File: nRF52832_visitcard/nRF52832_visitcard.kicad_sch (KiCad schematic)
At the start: 65 parts, among them J1 Programming, J2 UART, SW1 SW_Push, Y1 32 MHz

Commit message: Added LCSC to all the components
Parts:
- BT1: LCSC (none) -> C70373
- C1, C4, C8: LCSC (none) -> C1525
- C10: LCSC (none) -> C1705
- C11: footprint Capacitor_SMD:C_0402_1005Metric_Pad0.74x0.62mm_HandSolder -> Capacitor_SMD:C_0805_2012Metric_Pad1.18x1.45mm_HandSolder; LCSC (none) -> C1711
- C12: LCSC (none) -> C1691
- C13, C14: LCSC (none) -> C1546
- C2: LCSC (none) -> C23687
- C3: LCSC (none) -> C15684
- C5, C6: LCSC (none) -> C26406
- C7: LCSC (none) -> C126516
- C9: LCSC (none) -> C1606
- D1, D10, D11, D12, D13, D14, D15, D16, D17, D18, D2, D3, D4, D5, D6, D7, D8, D9: LCSC (none) -> C5197644
- L1: LCSC (none) -> C51942
- L2: LCSC (none) -> C23651
- L3: LCSC (none) -> C90202
- R1, R2: LCSC (none) -> C25992
- R10, R11, R12, R13, R14, R15, R16, R17, R18, R19, R20, R3, R4, R5, R6, R7, R8, R9: LCSC (none) -> C14676
- R21: LCSC (none) -> C15401
- U1: LCSC (none) -> C77540
- U2: LCSC (none) -> C976032
- Y1: LCSC (none) -> C5830663

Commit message: LCSC added to another component
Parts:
- SW1: LCSC (none) -> C499301
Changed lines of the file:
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@@
+      (effects (font (size 1.27 1.27)) hide)
+    )
+    (property "LCSC" "C499301" (at 201.93 138.43 90)
       (effects (font (size 1.27 1.27)) hide)
     )

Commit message: Board layout fix
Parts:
- C15: now not fitted
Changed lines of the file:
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@@
   )
   (symbol (lib_id "Device:C") (at 143.51 139.7 0) (unit 1)
-    (in_bom yes) (on_board yes) (dnp no)
+    (in_bom yes) (on_board yes) (dnp yes)
     (property "Reference" "C15" (at 139.7 139.7 90)
       (effects (font (size 1.27 1.27)))

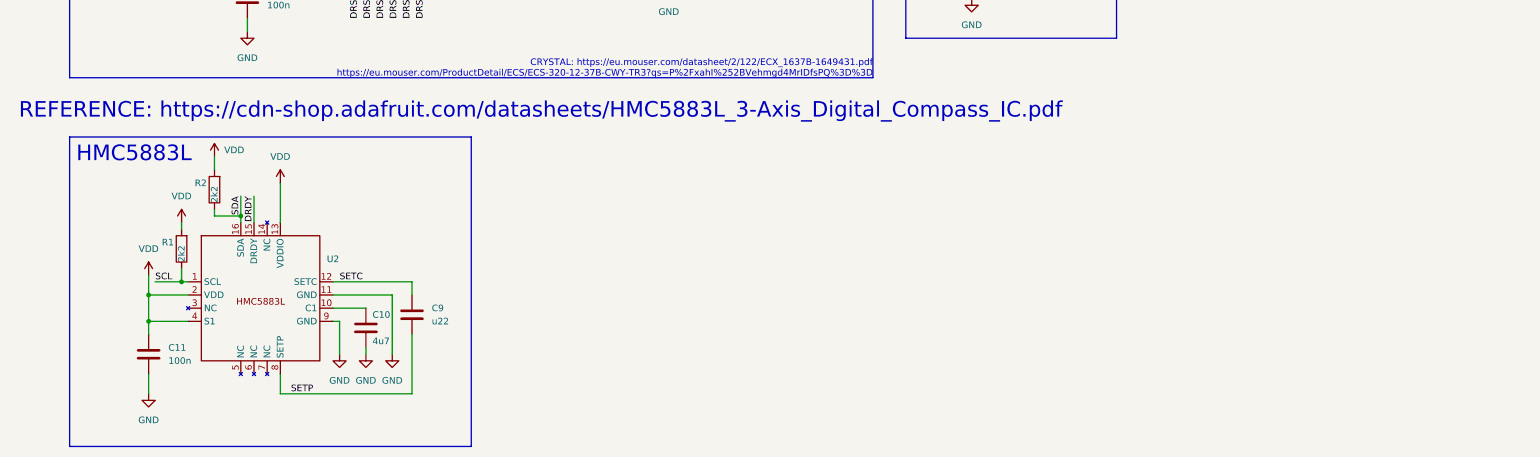
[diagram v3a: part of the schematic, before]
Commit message: Using QMC5833L instead of HMC5883L
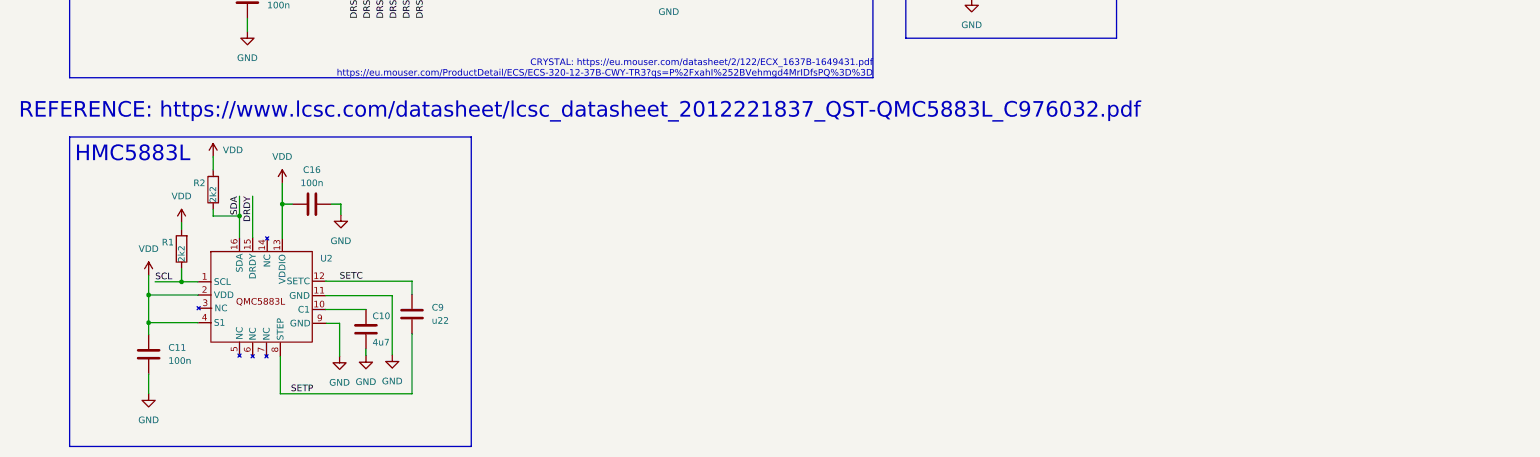
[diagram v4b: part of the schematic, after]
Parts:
- removed U2: ~, HMC5883L:HMC5883L, symbol HMC5883L:HMC5883L
- added C16: 100n, Capacitor_SMD:C_0805_2012Metric_Pad1.18x1.45mm_HandSolder, symbol Device:C
- added U2: ~, Package_LGA:LGA-16_3x3mm_P0.5mm, symbol QMC5883L:QMC5883L
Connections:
- net DRDY: now also U2.15 (DRDY)
- net GND: now also C16.2, U2.11 (GND), U2.9 (GND)
- net SCL: now also U2.1 (SCL)
- net SDA: now also U2.16 (SDA)
- net SETC: now also U2.12 (SETC)
- net SETP: now also U2.8 (STEP)
- net VDD: now also C16.1, U2.13 (VDDIO), U2.2 (VDD), U2.4 (S1)
- net at C10.1: now also U2.10 (C1)
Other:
- note added: "REFERENCE: https://www.lcsc.com/datasheet/lcsc_datasheet_2012221837_QST-QMC5883L_C976032.pdf"
- note removed: "REFERENCE: https://cdn-shop.adafruit.com/datasheets/HMC5883L_3-Axis_Digital_Compass_IC.pdf"

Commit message: PCB details - Rotated battery holder in 3D view - Silkscreen fix
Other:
- note added: "QMC5883L"
- note removed: "HMC5883L"
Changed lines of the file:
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@@
     (effects (font (size 3 3)) (justify left bottom))
   )
-  (text "HMC5883L" (at 28.956 180.34 0)
+  (text "QMC5883L" (at 28.956 180.34 0)
     (effects (font (size 3 3)) (justify left bottom))
   )
